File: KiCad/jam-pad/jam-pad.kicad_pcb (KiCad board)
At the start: 2 copper layers, 133.7 x 57.1 mm, 78 parts, among them J1 USB_C, J2 PH_01x03_2.54mm, SW1 MX_Hotswap_LED_RGB, SW13 SW_Push, SW14 RotaryEncoder_Switch, SW15 SW_Push, SW2 MX_Hotswap_LED_RGB, SW3 MX_Hotswap_LED_RGB, SW4 MX_Hotswap_LED_RGB, SW5 MX_Hotswap_LED_RGB, SW6 MX_Hotswap_LED_RGB, SW7 MX_Hotswap_LED_RGB, SW8 MX_Hotswap_LED_RGB, SW9 MX_Hotswap_LED_RGB, U1 RP2040, U3 W25Q16JVSNIQ, U4 MIC5319-3.3YD5, Y1 ECS-120-18-33-JGN

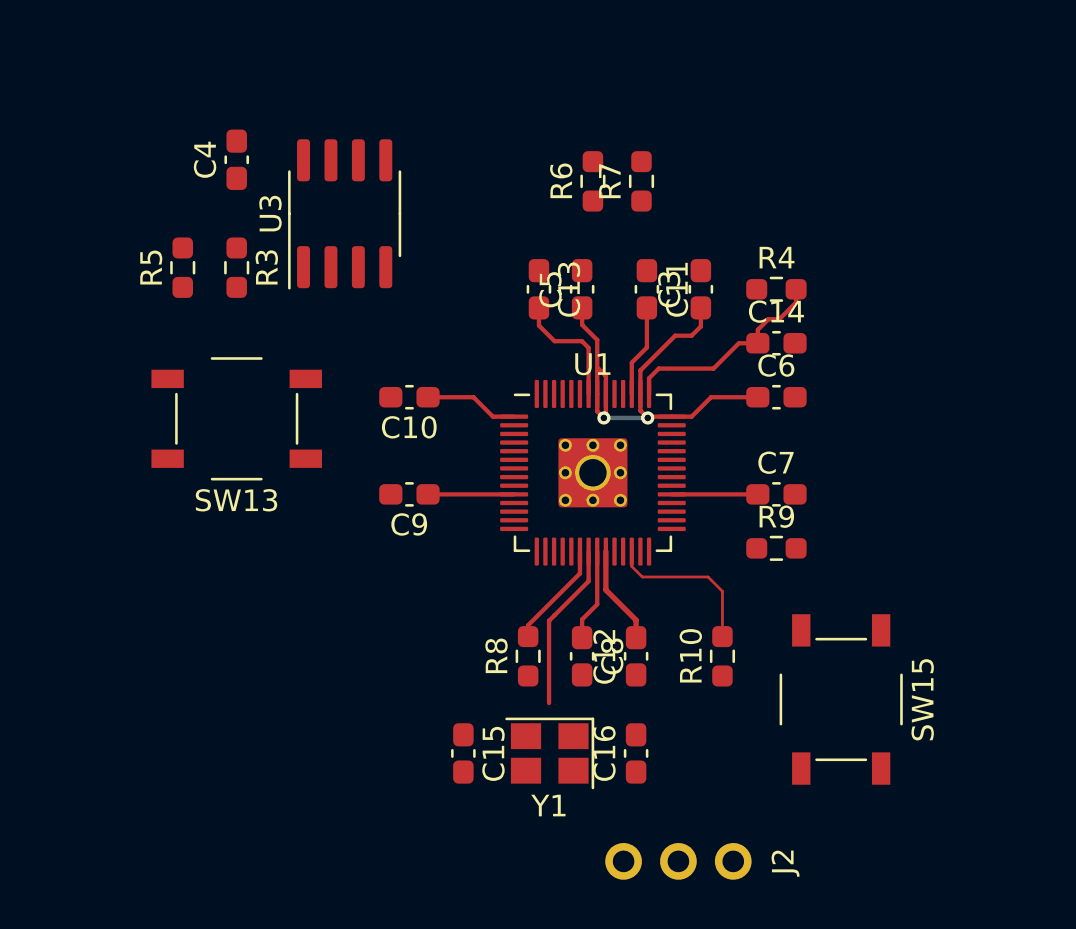
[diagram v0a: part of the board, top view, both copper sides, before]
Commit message: idk how to route + forgot to put flipped led switch fp in
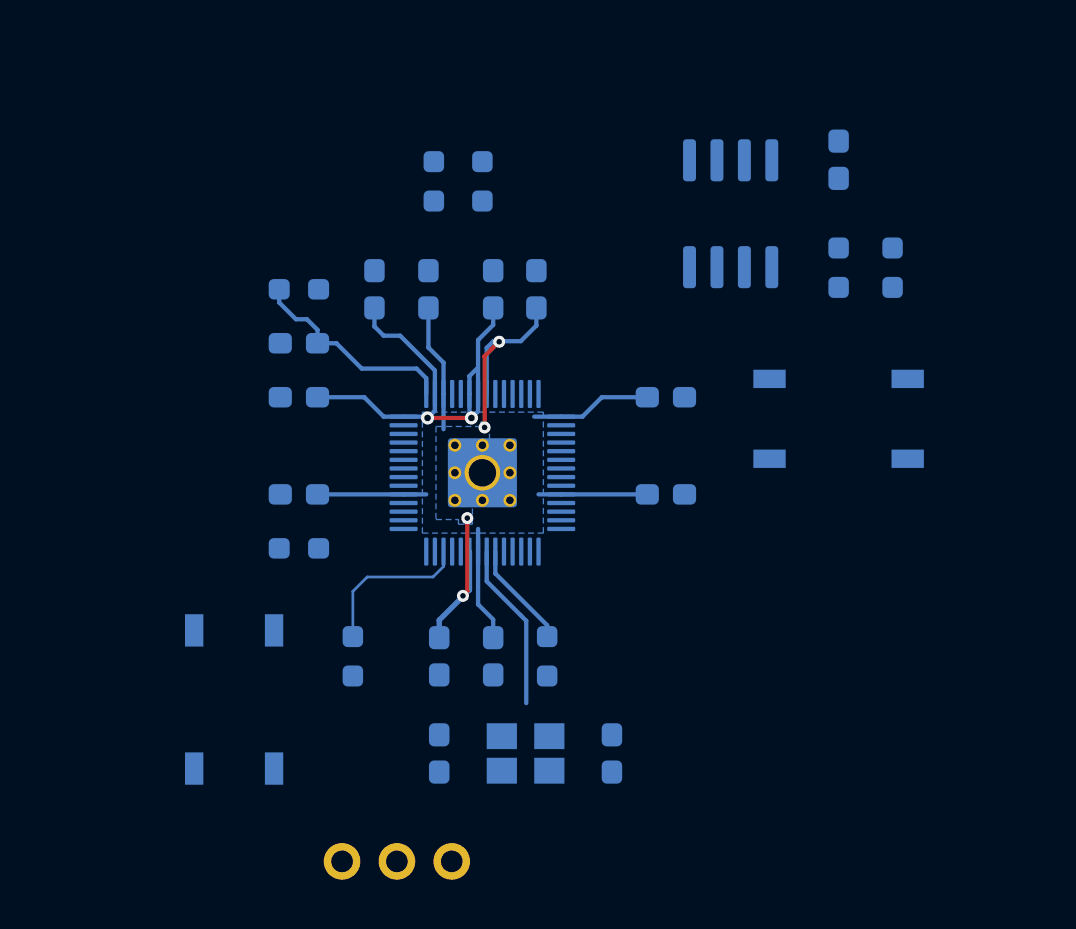
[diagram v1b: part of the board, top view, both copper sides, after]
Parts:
- C10, C11, C12, C13, C14, C15, C16, C3, C4, C5, C6, C7, C8, C9, J2, R10, R3, R4, R5, R6, R7, R8, R9, SW13, SW15, U1, U3, Y1: moved to B.Cu
- moved R5 32.9 mm to (81.8, 133.4)
- moved SW15 28.1 mm to (51.3, 153.4)
- moved C4 27.9 mm to (79.3, 128.4)
- moved R3 27.9 mm to (79.3, 133.4)
- moved SW13 27.9 mm to (79.3, 140.4), turned to 0 degrees
- moved C14 22.1 mm to (54.3, 136.9), turned to 180 degrees
- moved C6 22.1 mm to (54.3, 139.4), turned to 180 degrees
- moved C7 22.1 mm to (54.3, 143.9), turned to 180 degrees
- moved R4 22.1 mm to (54.3, 134.4), turned to 180 degrees
- moved R9 22.1 mm to (54.3, 146.4), turned to 180 degrees
- moved J2 18.1 mm to (56.3, 160.9)
- moved U3 17.9 mm to (74.3, 130.9)
- moved R10 17.1 mm to (56.8, 151.4)
- moved C3 15.1 mm to (57.8, 134.4)
- moved C10 11.9 mm to (71.3, 139.4), turned to 0 degrees
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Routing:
- net +1V1: track 14.5 -> 24.1 mm, vias 0 -> 4
- net +3V3: track 78.5 -> 82.9 mm
- added copper zone on B.Cu, net +1V1
- added copper zone on B.Cu, net +3V3

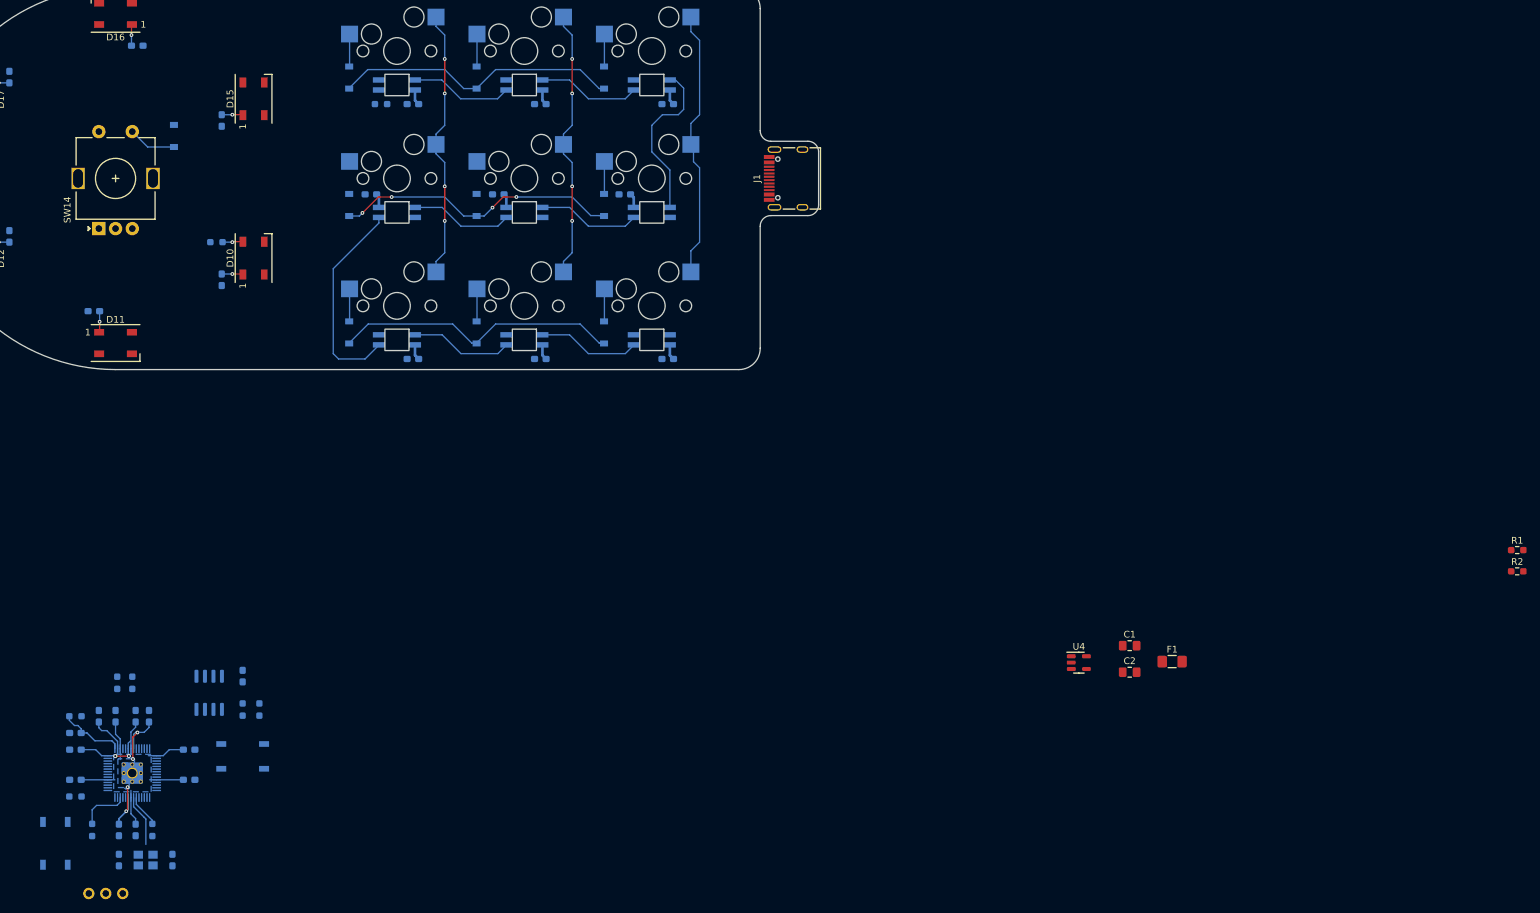
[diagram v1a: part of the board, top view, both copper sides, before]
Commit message: mcu placing + routing, power LED on 5V and level shifter
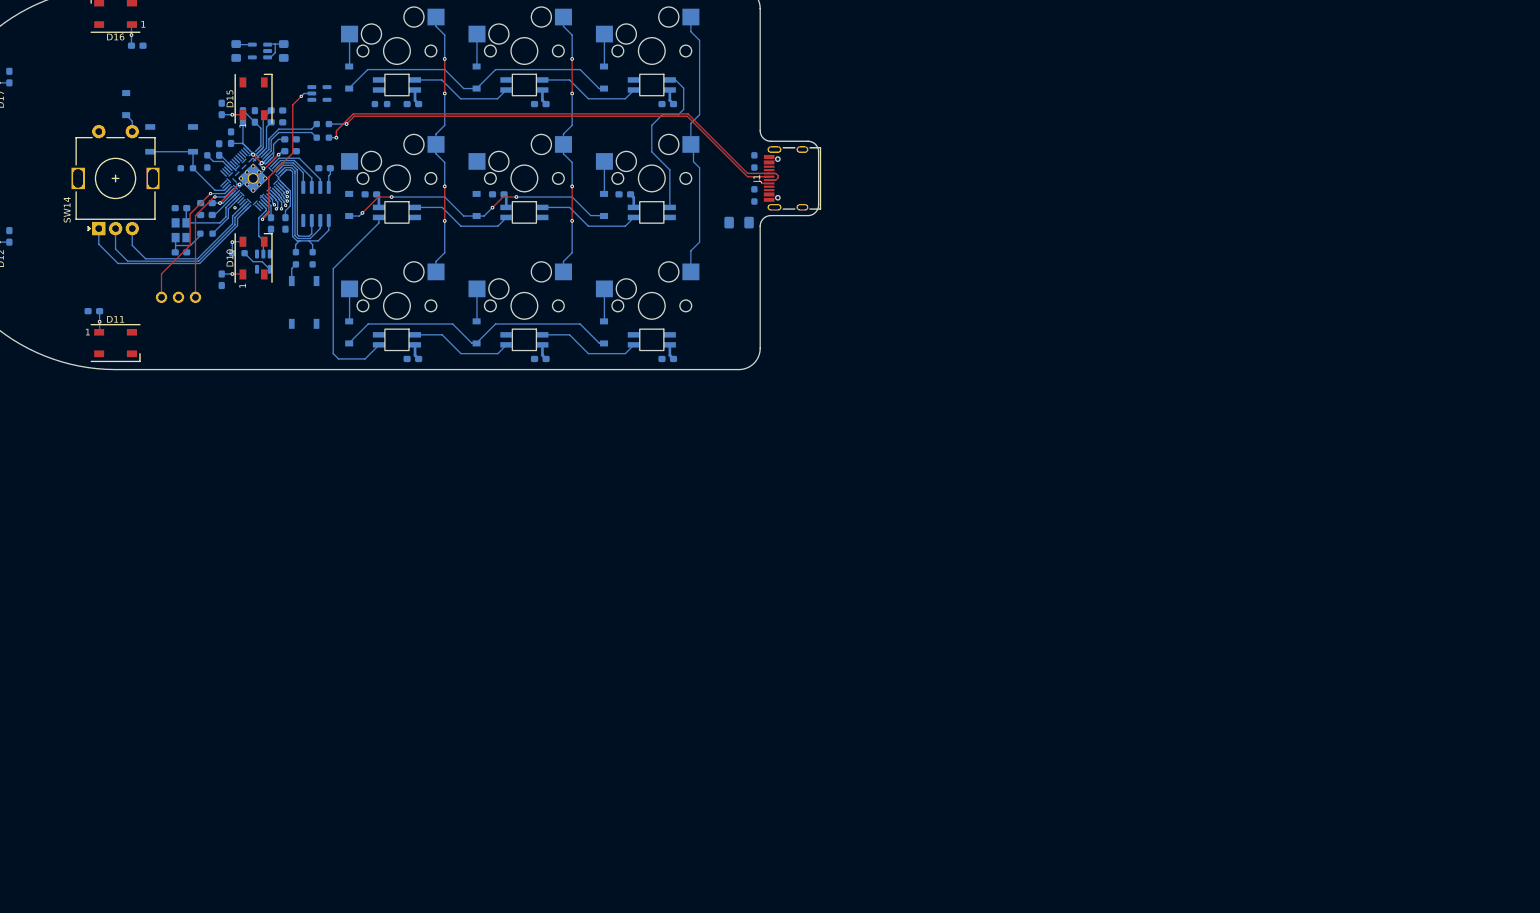
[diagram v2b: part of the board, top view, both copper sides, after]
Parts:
- added U2: SN74LV1T34DBV, Package_TO_SOT_SMD:SOT-23-5, B.Cu at (90.8, 41.3)
- added U5: SN74LV1T34DBV, Package_TO_SOT_SMD:SOT-23-5, B.Cu at (82.4, 66.4)
- C1, C2, F1, R1, R2, U4: moved to B.Cu
- moved C2 162.7 mm to (78.4, 34.9), turned to -90 degrees
- moved C1 154.6 mm to (85.5, 34.9), turned to -90 degrees
- moved U4 152.8 mm to (81.9, 34.9), turned to 180 degrees
- moved R1 128.0 mm to (155.8, 51.4), turned to 90 degrees
- moved R2 127.1 mm to (155.8, 56.5), turned to -90 degrees
- moved SW15 106.7 mm to (68.7, 48.1), turned to 180 degrees
- moved R10 99.9 mm to (71.0, 52.5), turned to 0 degrees
- moved C16 97.9 mm to (70.1, 58.4), turned to 0 degrees
- moved R9 97.0 mm to (74.0, 51.4), turned to -90 degrees
- moved C7 96.6 mm to (75.8, 49.7), turned to 90 degrees
- moved C14 96.0 mm to (81.2, 44.7), turned to 90 degrees
- moved C12 94.6 mm to (73.9, 57.7), turned to 0 degrees
- moved C6 94.4 mm to (77.6, 47.9), turned to 90 degrees
- moved C3 94.4 mm to (84.5, 43.8), turned to 0 degrees
- moved Y1 94.3 mm to (70.1, 61.7), turned to -90 degrees
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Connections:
- C17 pad 1: +3V3 -> +5V
- C18 pad 1: +3V3 -> +5V
- C19 pad 1: +3V3 -> +5V
- C20 pad 1: +3V3 -> +5V
- C21 pad 1: +3V3 -> +5V
- C22 pad 1: +3V3 -> +5V
- C23 pad 1: +3V3 -> +5V
- C24 pad 1: +3V3 -> +5V
- C25 pad 1: +3V3 -> +5V
- C26 pad 2: +3V3 -> +5V
- C27 pad 2: +3V3 -> +5V
- C28 pad 2: +3V3 -> +5V
- C30 pad 2: +3V3 -> +5V
- C31 pad 2: +3V3 -> +5V
- C32 pad 2: +3V3 -> +5V
- D10 pad 1: +3V3 -> +5V
- D11 pad 1: +3V3 -> +5V
- D12 pad 1: +3V3 -> +5V
- D15 pad 1: +3V3 -> +5V
- D16 pad 1: +3V3 -> +5V
- D17 pad 1: +3V3 -> +5V
- SW1 pad 3: +3V3 -> +5V
- SW2 pad 3: +3V3 -> +5V
- SW3 pad 3: +3V3 -> +5V
- SW4 pad 3: +3V3 -> +5V
- SW5 pad 3: +3V3 -> +5V
- SW6 pad 3: +3V3 -> +5V
- SW7 pad 3: +3V3 -> +5V
- SW8 pad 3: +3V3 -> +5V
- SW9 pad 3: +3V3 -> +5V
- U1 pad 11: /Backlight -> /Backlight_3V3
- U1 pad 12: /Knob_Light -> /Knob_Light_3V3
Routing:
- net /USB_D+: track 0.00 -> 74.9 mm, vias 0 -> 1
- net /USB_D-: track 0.00 -> 72.2 mm, vias 0 -> 1
- net +5V: track 0.00 -> 44.8 mm
- net +3V3: track 82.9 -> 51.8 mm
- net /ENC_A: track 0.00 -> 29.9 mm
- net /ENC_C: track 0.00 -> 27.4 mm
- net /Backlight_3V3: track 0.00 -> 25.8 mm, vias 0 -> 2
- net /ENC_B: track 0.00 -> 24.2 mm
- net /QSPI_SS: track 0.00 -> 23.1 mm
- net /SWDIO: track 0.00 -> 21.6 mm, vias 0 -> 1
- net /SWCLK: track 0.00 -> 19.1 mm, vias 0 -> 1
- net /QSPI_SD1: track 0.00 -> 18.0 mm
- net /QSPI_SD2: track 0.00 -> 17.3 mm
- net /D-: track 0.00 -> 10.7 mm
- net /D+: track 0.00 -> 10.4 mm
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
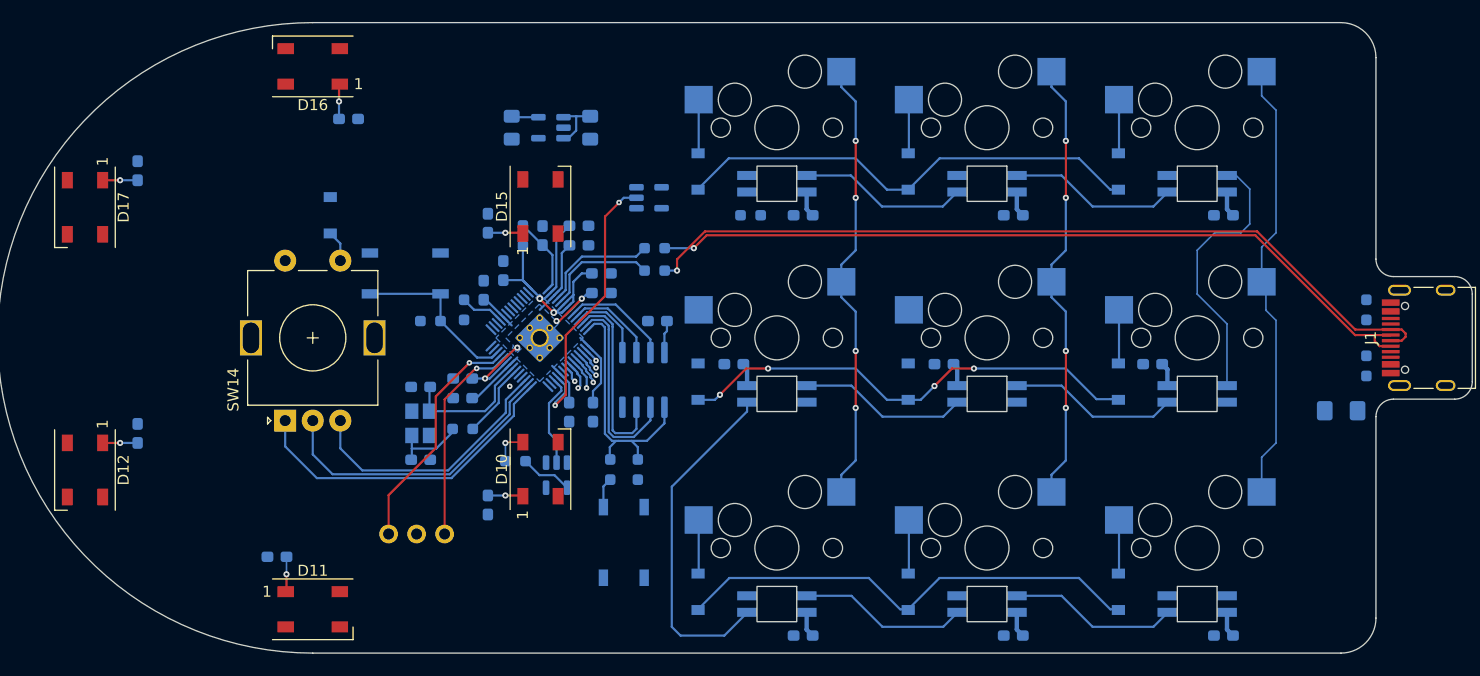
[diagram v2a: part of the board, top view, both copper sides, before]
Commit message: bit of power routing
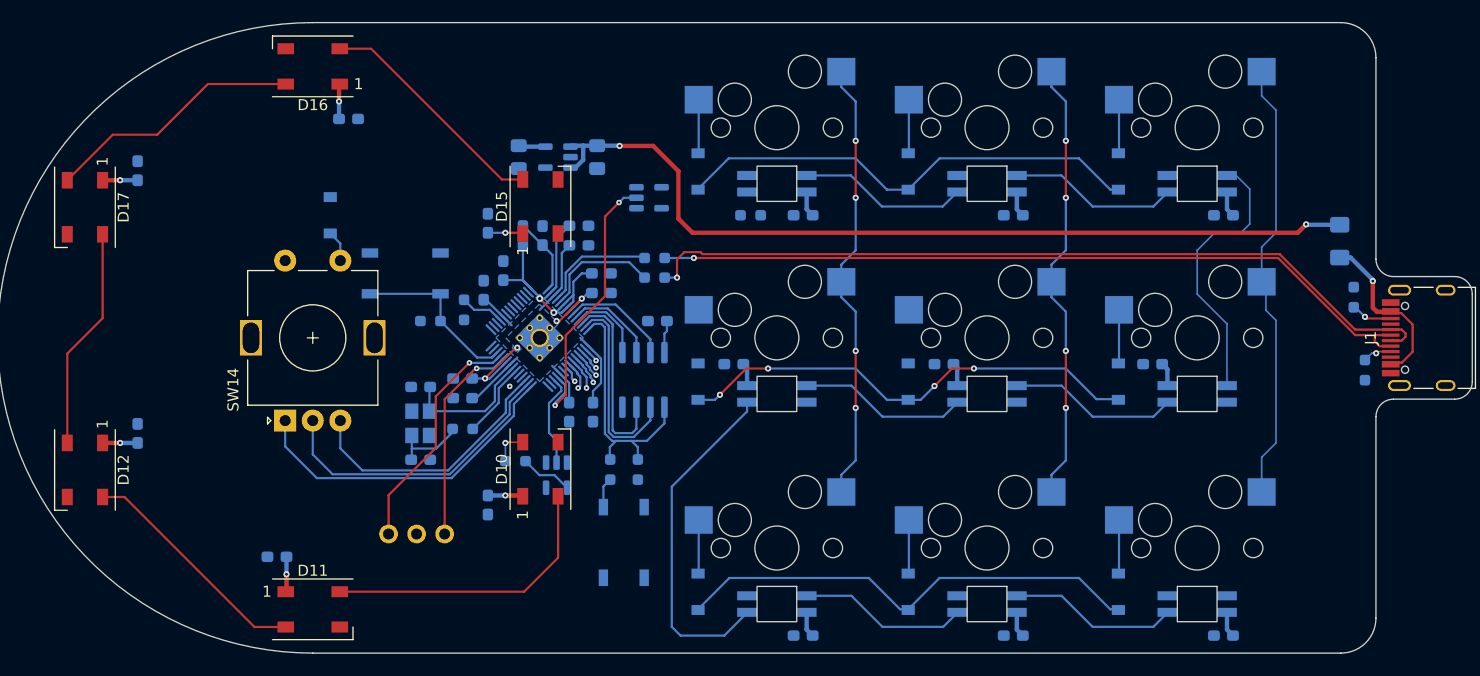
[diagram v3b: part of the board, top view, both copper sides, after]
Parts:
- moved F1 15.4 mm to (153.4, 45.2), turned to 90 degrees
- moved C2 2.74 mm to (79.0, 37.6)
- moved C1 2.74 mm to (86.1, 37.6)
- moved U4 2.74 mm to (82.5, 37.6)
- moved R1 1.62 mm to (154.7, 50.3)
- moved R7 0.89 mm to (91.3, 46.7)
- moved R6 0.64 mm to (91.3, 48.5)
- moved R2 0.40 mm to (155.7, 56.9)
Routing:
- net +5V: track 44.8 -> 118.2 mm, vias 0 -> 8
- net Net-(D10-DOUT): track 0.00 -> 26.6 mm
- net Net-(D16-DIN): track 0.00 -> 23.4 mm
- net Net-(D15-DIN): track 0.00 -> 21.5 mm
- net Net-(D11-DOUT): track 0.00 -> 21.5 mm
- net Net-(D12-DOUT): track 0.00 -> 20.2 mm
- net VUSB: track 0.00 -> 15.4 mm, vias 0 -> 1
- net Net-(J1-CC2): track 0.00 -> 3.77 mm, vias 0 -> 1
- net Net-(J1-CC1): track 0.00 -> 2.65 mm, vias 0 -> 1
- net /USB_D-: track 72.2 -> 70.9 mm
- net /USB_D+: track 74.9 -> 73.9 mm
- net +3V3: vias 8 -> 2

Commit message: finished everything besides ground preliminarily
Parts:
- moved D13 3.44 mm to (65.0, 41.4)
- moved C24 2.89 mm to (126.6, 80.2), turned to 90 degrees
- moved C23 2.89 mm to (107.6, 80.2), turned to 90 degrees
- moved C25 2.89 mm to (145.7, 80.2), turned to 90 degrees
- moved R11 1.19 mm to (98.8, 42.9)
- moved R2 1.02 mm to (154.7, 56.9)
- moved U2 0.08 mm to (90.9, 41.3)
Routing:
- net +5V: track 118.2 -> 424.6 mm, vias 8 -> 17
- net Col0: track 43.1 -> 134.5 mm, vias 5 -> 9
- net Col2: track 43.5 -> 111.8 mm, vias 1 -> 4
- net Row0: track 44.3 -> 102.4 mm, vias 1 -> 2
- net Col1: track 43.2 -> 91.4 mm, vias 5 -> 8
- net Row2: track 45.3 -> 70.8 mm, vias 1 -> 3
- net Col3: track 1.52 -> 18.7 mm, vias 1 -> 3
- net Row1: track 44.7 -> 57.5 mm, vias 5 -> 6
- net /Backlight: track 0.00 -> 6.94 mm, vias 0 -> 2
- net Net-(SW1B-DIN): track 0.00 -> 2.12 mm
- net Net-(D13-A): track 2.84 -> 4.83 mm
- net Net-(SW4B-DOUT): track 31.7 -> 30.6 mm
- net Net-(J1-CC1): track 2.65 -> 3.66 mm

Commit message: initial plate stuff
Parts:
- moved J1 2.31 mm to (156.5, 54.0)
- moved R1 2.31 mm to (152.4, 50.3)
- moved R2 2.31 mm to (152.4, 56.9)
- moved F1 2.29 mm to (151.1, 45.2)
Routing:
- net +5V: track 424.6 -> 422.3 mm
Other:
- board size 133.7 x 57.1 mm -> 131.6 x 57.1 mm

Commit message: routing adjustments, ec11 standoff, need to fix drc kms
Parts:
- added REF**: MountingHole_2.2mm_M2_Pad, MountingHole:MountingHole_2.2mm_M2_Pad, F.Cu at (60.3, 38.5)
- added REF**: MountingHole_2.2mm_M2_Pad, MountingHole:MountingHole_2.2mm_M2_Pad, F.Cu at (60.3, 69.8)
- C1, C2: value 10u -> 10uF
- C10, C12, C13, C4, C5, C6, C7, C8, C9: value 100n -> 0.1uF
- C11, C14, C3: value 2.2u -> 2.2uF
- C17, C18, C19, C20, C21, C22, C23, C24, C25, C26, C27, C28, C30, C31, C32: value .1u -> 0.1uF
- moved SW13 3.18 mm to (88.5, 69.3)
- moved J2 3.00 mm to (68.1, 74.6)
- moved R3 2.79 mm to (90.3, 63.2)
- moved R5 2.79 mm to (87.8, 63.2)
- moved U3 2.10 mm to (90.9, 55.8)
- moved C4 1.83 mm to (91.7, 50.6)
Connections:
- SW14 pad S2: Col0 -> Col3
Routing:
- net Col0: track 134.5 -> 74.3 mm, vias 9 -> 6
- net +3V3: track 51.8 -> 105.7 mm, vias 2 -> 4
- net Col3: track 18.7 -> 49.8 mm
- net Row0: track 102.4 -> 114.8 mm
- net /SWCLK: track 19.1 -> 31.4 mm
- net /SWDIO: track 21.6 -> 28.6 mm
- net /~{USB_BOOT}: track 2.75 -> 9.42 mm
- net Net-(D4-A): track 0.00 -> 4.88 mm
- net Row1: track 57.5 -> 62.3 mm
- net +5V: track 422.3 -> 427.0 mm
- net Col2: track 111.8 -> 116.2 mm, vias 4 -> 2
- net Col1: track 91.4 -> 94.9 mm, vias 8 -> 6
- net /QSPI_SD2: track 17.3 -> 14.6 mm
- net Row2: track 70.8 -> 73.4 mm, vias 3 -> 5
- net /QSPI_SS: track 23.1 -> 20.9 mm
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- added copper zone on B.Cu, net GND
- added copper zone on F.Cu, net GND
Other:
- board size 131.6 x 57.1 mm -> 131.4 x 57.1 mm
